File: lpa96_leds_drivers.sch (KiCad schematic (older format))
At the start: 115 parts, among them U3 TLC5941, U4 TLC5941, U5 TLC5941, U6 TLC5941, U7 TLC5941, U8 TLC5941

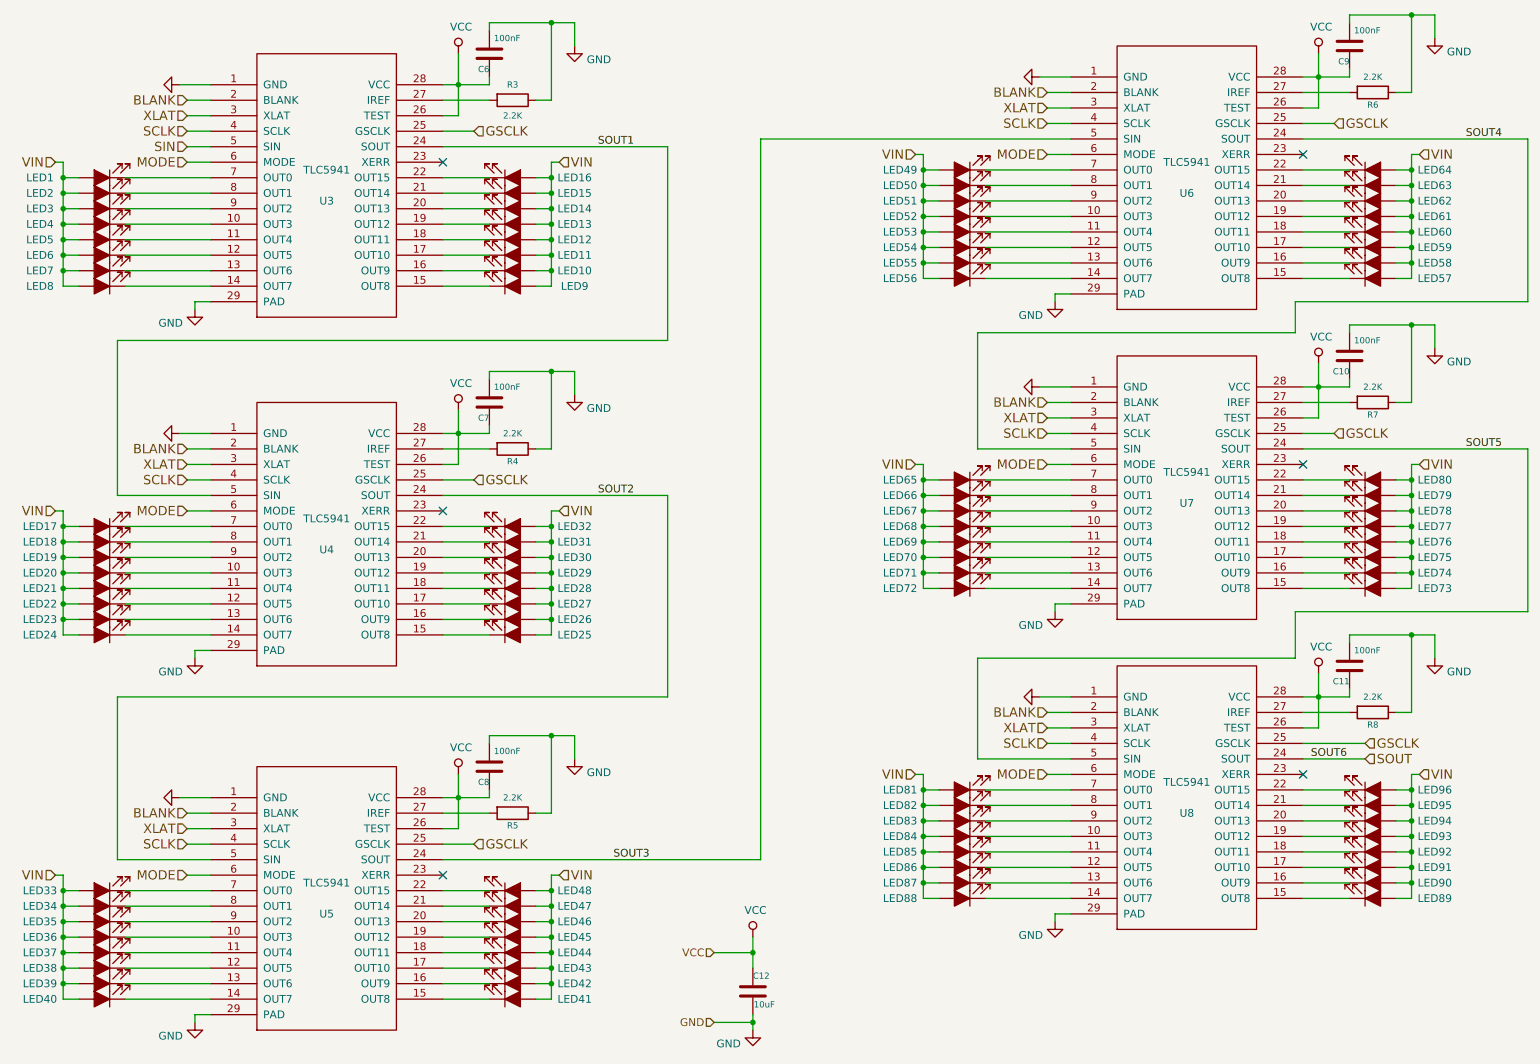
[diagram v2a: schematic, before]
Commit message: small tweaks, added component part numbers & descriptions into design
added all part info from original 24well LPA 'Nature' article (Supplementary Information, Table S1).
part info uses "Description", "Manufacturer1", "MPN1", "Vendor1" and "SKU1" part fields.
changed part info for new LED parts, and C5,C12 chosen part for new case size.
changed P2 to 2x3way exact part rather than 40way breakable header.
changed R15-R19 from 50k to 47k to match part number
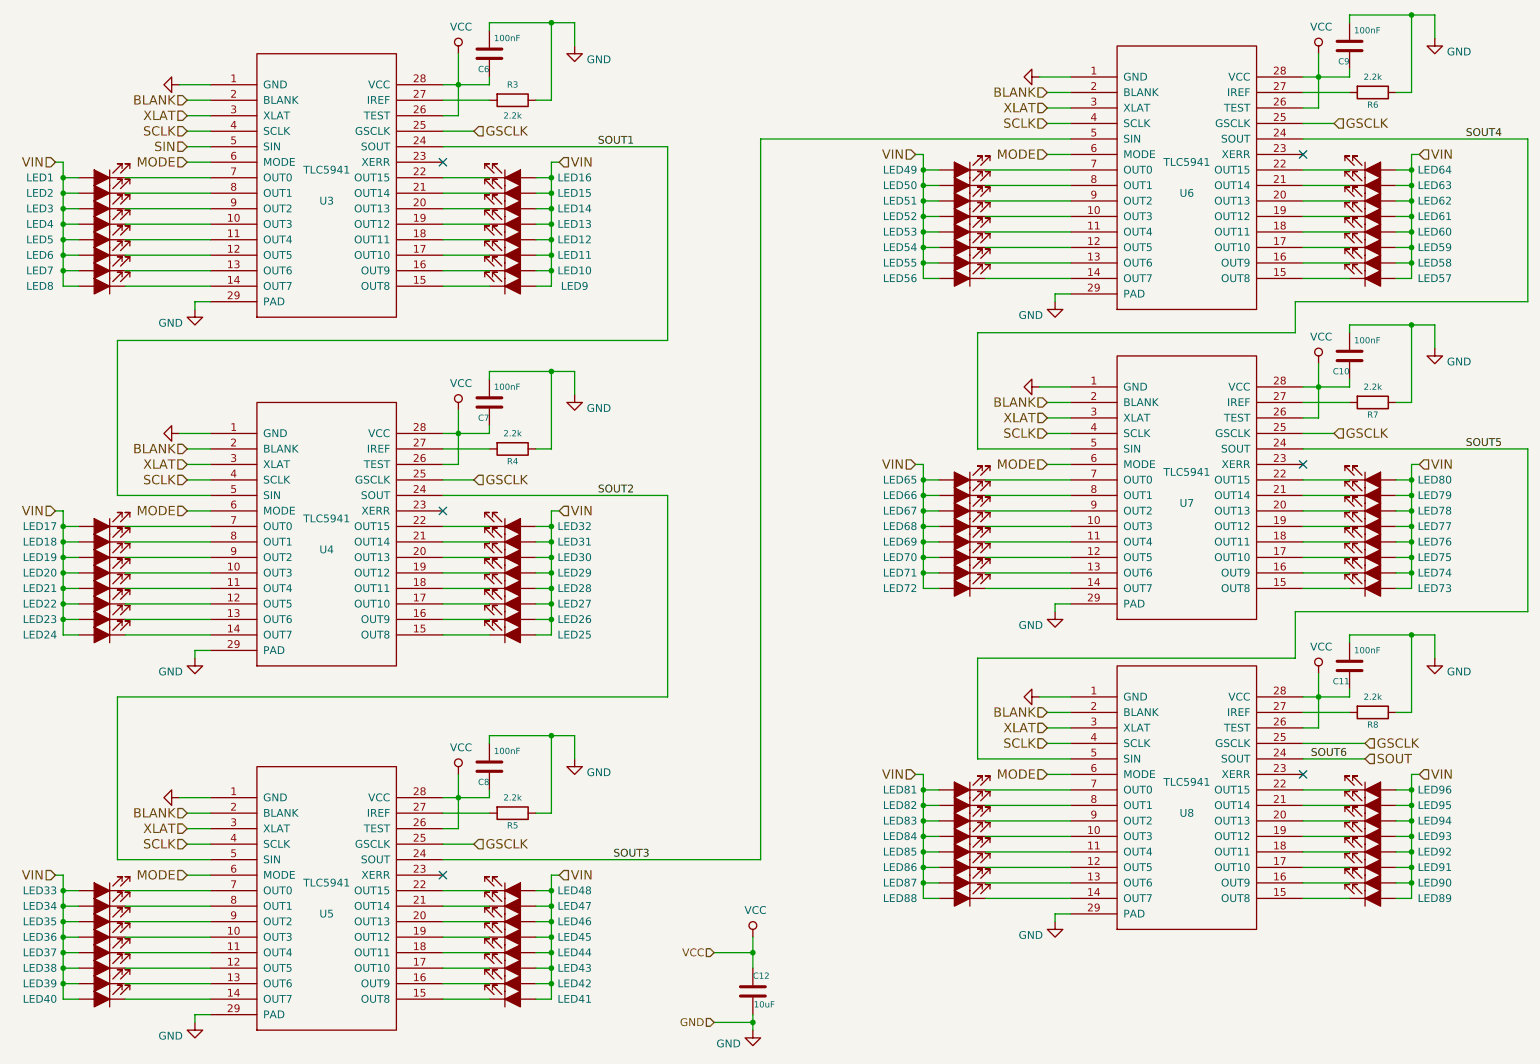
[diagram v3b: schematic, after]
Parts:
- C10, C11, C6, C7, C8, C9: Description (none) -> -20/+80% 50V Y5V SMD MLCC Capacitor 0805; MPN1 (none) -> CL21F104ZBCNNNC; Manufacturer1 (none) -> Samsung; SKU1 (none) -> 1276-1007-1-ND; Vendor1 (none) -> Digikey
- C12: Description (none) -> 10% 25V X5R SMD MLCC Capacitor 1206; MPN1 (none) -> CL31A106KAHNNNE; Manufacturer1 (none) -> Samsung; SKU1 (none) -> 1276-1075-1-ND; Vendor1 (none) -> Digikey
- LED1, LED10, LED11, LED12, LED13, LED14, LED15, LED16, LED17, LED18, LED19, LED2, LED20, LED21, LED22, LED23, LED24, LED25, LED26, LED27, LED28, LED29, LED3, LED30, LED31, LED32, LED33, LED34, LED35, LED36, LED37, LED38, LED39, LED4, LED40, LED41, LED42, LED43, LED44, LED45, LED46, LED47, LED48, LED49, LED5, LED50, LED51, LED52, LED53, LED54, LED55, LED56, LED57, LED58, LED59, LED6, LED60, LED61, LED62, LED63, LED64, LED65, LED66, LED67, LED68, LED69, LED7, LED70, LED71, LED72, LED73, LED74, LED75, LED76, LED77, LED78, LED79, LED8, LED80, LED81, LED82, LED83, LED84, LED85, LED86, LED87, LED88, LED89, LED9, LED90, LED91, LED92, LED93, LED94, LED95, LED96: Description (none) -> Blue 465nm LED 3V 2-SMD, Gull Wing; MPN1 (none) -> VLDB1232G-08; Manufacturer1 (none) -> Vishay; SKU1 (none) -> VLDB1232G-08CT-ND; Vendor1 (none) -> Digikey
- R3, R4, R5, R6, R7, R8: value 2.2K -> 2.2k; Description (none) -> 0.5% Chip Resistor 0805; MPN1 (none) -> RR1220P-222-D; Manufacturer1 (none) -> Susumu; SKU1 (none) -> RR12P2.2KDCT-ND; Vendor1 (none) -> Digikey
- U3, U4, U5, U6, U7, U8: Description (none) -> LED Driver IC 16 Output 28-HTSSOP; MPN1 (none) -> TLC5941PWP; Manufacturer1 (none) -> Texas Instruments; SKU1 (none) -> 296-18617-5-ND; Vendor1 (none) -> Digikey

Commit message: updated 3d models & footprint references
changed P1 and P2 library part models to match part from BOM
added Molex step model for P1
fixed U2 SOT223 model to use modern STEP model instead of old .wrl
updated resistor/capacitor footprints to match KiCAD5 library name changes
deleted fp-info-cache and added to git ignore (not needed, generated dynamically)
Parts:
- C10, C11, C6, C7, C8, C9: footprint Capacitors_SMD:C_0805 -> Capacitor_SMD:C_0805_2012Metric
- C12: footprint Capacitors_SMD:C_1206 -> Capacitor_SMD:C_1206_3216Metric
- R3, R4, R5, R6, R7, R8: footprint Resistors_SMD:R_0805 -> Resistor_SMD:R_0805_2012Metric
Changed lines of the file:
@@
 F 0 "R5" V 4280 5700 40  0000 C CNN
 F 1 "2.2k" V 4100 5700 40  0000 C CNN
-F 2 "Resistors_SMD:R_0805" V 4130 5700 30  0001 C CNN
+F 2 "Resistor_SMD:R_0805_2012Metric" V 4130 5700 30  0001 C CNN
 F 3 "~" H 4200 5700 30  0000 C CNN
 F 4 "0.5% Chip Resistor 0805" H 4200 5700 50  0001 C CNN "Description"
@@
 F 0 "R4" V 4280 3350 40  0000 C CNN
 F 1 "2.2k" V 4100 3350 40  0000 C CNN
-F 2 "Resistors_SMD:R_0805" V 4130 3350 30  0001 C CNN
+F 2 "Resistor_SMD:R_0805_2012Metric" V 4130 3350 30  0001 C CNN
 F 3 "~" H 4200 3350 30  0000 C CNN
 F 4 "0.5% Chip Resistor 0805" H 4200 3350 50  0001 C CNN "Description"
@@
 F 0 "R3" V 4100 1100 40  0000 C CNN
 F 1 "2.2k" V 4300 1100 40  0000 C CNN
-F 2 "Resistors_SMD:R_0805" V 4130 1100 30  0001 C CNN
+F 2 "Resistor_SMD:R_0805_2012Metric" V 4130 1100 30  0001 C CNN
 F 3 "~" H 4200 1100 30  0000 C CNN
 F 4 "0.5% Chip Resistor 0805" H 4200 1100 50  0001 C CNN "Description"
@@
 F 0 "R8" V 9830 5050 40  0000 C CNN
 F 1 "2.2k" V 9650 5050 40  0000 C CNN
-F 2 "Resistors_SMD:R_0805" V 9680 5050 30  0001 C CNN
+F 2 "Resistor_SMD:R_0805_2012Metric" V 9680 5050 30  0001 C CNN
 F 3 "~" H 9750 5050 30  0000 C CNN
 F 4 "0.5% Chip Resistor 0805" H 9750 5050 50  0001 C CNN "Description"
@@
 F 0 "R6" V 9830 1050 40  0000 C CNN
 F 1 "2.2k" V 9650 1050 40  0000 C CNN
-F 2 "Resistors_SMD:R_0805" V 9680 1050 30  0001 C CNN
+F 2 "Resistor_SMD:R_0805_2012Metric" V 9680 1050 30  0001 C CNN
 F 3 "~" H 9750 1050 30  0000 C CNN
 F 4 "0.5% Chip Resistor 0805" H 9750 1050 50  0001 C CNN "Description"
@@
 F 0 "R7" V 9830 3050 40  0000 C CNN
 F 1 "2.2k" V 9650 3050 40  0000 C CNN
-F 2 "Resistors_SMD:R_0805" V 9680 3050 30  0001 C CNN
+F 2 "Resistor_SMD:R_0805_2012Metric" V 9680 3050 30  0001 C CNN
 F 3 "~" H 9750 3050 30  0000 C CNN
 F 4 "0.5% Chip Resistor 0805" H 9750 3050 50  0001 C CNN "Description"
@@
 F 0 "C12" H 5750 6950 40  0000 L CNN
 F 1 "10uF" H 5756 6765 40  0000 L CNN
-F 2 "Capacitors_SMD:C_1206" H 5788 6700 30  0001 C CNN
+F 2 "Capacitor_SMD:C_1206_3216Metric" H 5788 6700 30  0001 C CNN
 F 3 "~" H 5750 6850 60  0000 C CNN
 F 4 "10% 25V X5R SMD MLCC Capacitor 1206" H 5750 6850 50  0001 C CNN "Description"
@@
 F 0 "C11" H 9600 4850 40  0000 L CNN
 F 1 "100nF" H 9400 4650 40  0000 L CNN
-F 2 "Capacitors_SMD:C_0805" H 9638 4600 30  0001 C CNN
+F 2 "Capacitor_SMD:C_0805_2012Metric" H 9638 4600 30  0001 C CNN
 F 3 "~" H 9600 4750 60  0000 C CNN
 F 4 "-20/+80% 50V Y5V SMD MLCC Capacitor 0805" H 9600 4750 50  0001 C CNN "Description"
@@
 F 0 "C10" H 9600 2850 40  0000 L CNN
 F 1 "100nF" H 9400 2650 40  0000 L CNN
-F 2 "Capacitors_SMD:C_0805" H 9638 2600 30  0001 C CNN
+F 2 "Capacitor_SMD:C_0805_2012Metric" H 9638 2600 30  0001 C CNN
 F 3 "~" H 9600 2750 60  0000 C CNN
 F 4 "-20/+80% 50V Y5V SMD MLCC Capacitor 0805" H 9600 2750 50  0001 C CNN "Description"
@@
 F 0 "C9" H 9600 850 40  0000 L CNN
 F 1 "100nF" H 9400 650 40  0000 L CNN
-F 2 "Capacitors_SMD:C_0805" H 9638 600 30  0001 C CNN
+F 2 "Capacitor_SMD:C_0805_2012Metric" H 9638 600 30  0001 C CNN
 F 3 "~" H 9600 750 60  0000 C CNN
 F 4 "-20/+80% 50V Y5V SMD MLCC Capacitor 0805" H 9600 750 50  0001 C CNN "Description"
@@
 F 0 "C8" H 4050 5500 40  0000 L CNN
 F 1 "100nF" H 3850 5300 40  0000 L CNN
-F 2 "Capacitors_SMD:C_0805" H 4088 5250 30  0001 C CNN
+F 2 "Capacitor_SMD:C_0805_2012Metric" H 4088 5250 30  0001 C CNN
 F 3 "~" H 4050 5400 60  0000 C CNN
 F 4 "-20/+80% 50V Y5V SMD MLCC Capacitor 0805" H 4050 5400 50  0001 C CNN "Description"
@@
 F 0 "C7" H 4050 3150 40  0000 L CNN
 F 1 "100nF" H 3850 2950 40  0000 L CNN
-F 2 "Capacitors_SMD:C_0805" H 4088 2900 30  0001 C CNN
+F 2 "Capacitor_SMD:C_0805_2012Metric" H 4088 2900 30  0001 C CNN
 F 3 "~" H 4050 3050 60  0000 C CNN
 F 4 "-20/+80% 50V Y5V SMD MLCC Capacitor 0805" H 4050 3050 50  0001 C CNN "Description"
@@
 F 0 "C6" H 4050 900 40  0000 L CNN
 F 1 "100nF" H 3850 700 40  0000 L CNN
-F 2 "Capacitors_SMD:C_0805" H 4088 650 30  0001 C CNN
+F 2 "Capacitor_SMD:C_0805_2012Metric" H 4088 650 30  0001 C CNN
 F 3 "~" H 4050 800 60  0000 C CNN
 F 4 "-20/+80% 50V Y5V SMD MLCC Capacitor 0805" H 4050 800 50  0001 C CNN "Description"
